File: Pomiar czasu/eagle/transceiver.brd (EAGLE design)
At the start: 100.3 x 59.6 mm, 61 parts, among them IC1 MEGA8-AI, U1 RFM69HW

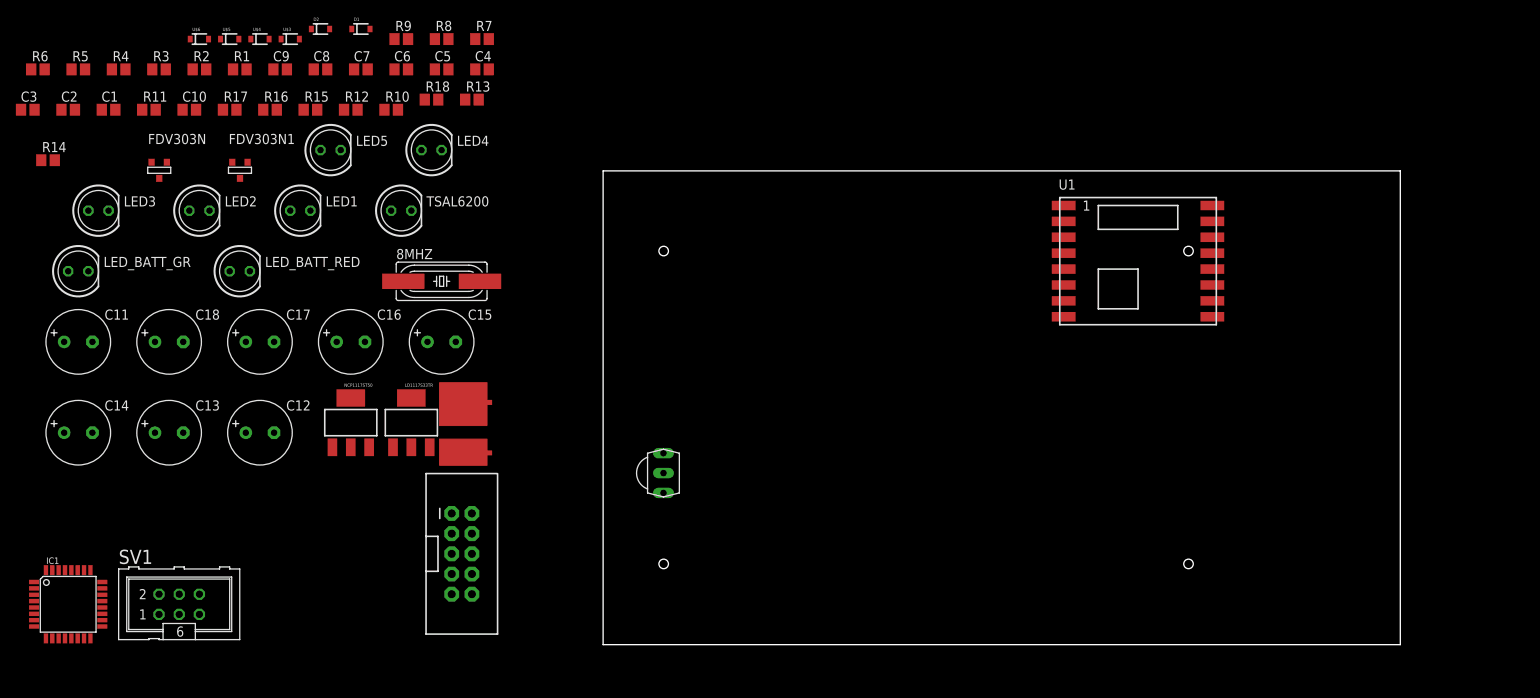
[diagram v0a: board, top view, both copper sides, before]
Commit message: defines added, demo program
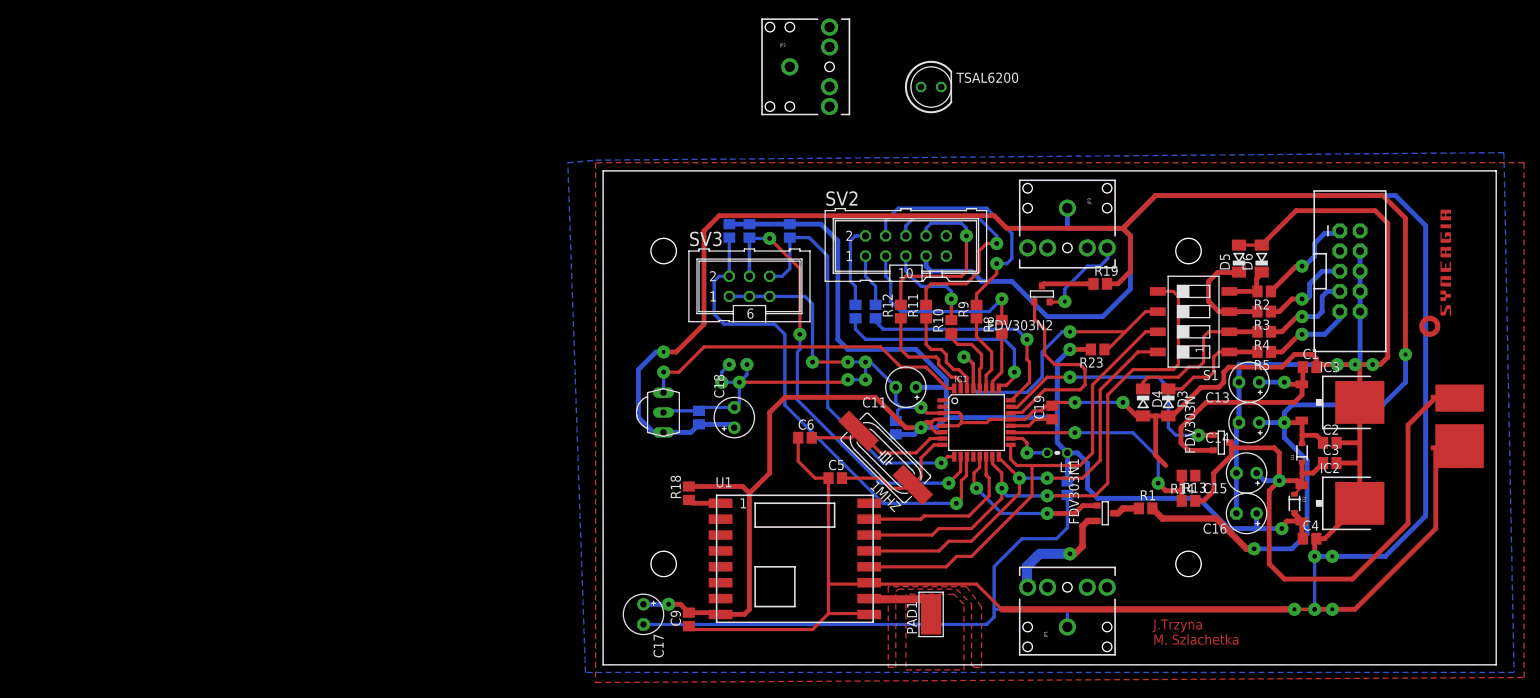
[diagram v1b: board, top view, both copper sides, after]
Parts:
- removed 8MHZ: (no value), crystal:HC49UP
- removed C12: (no value), resistor:E3,5-8
- removed C8: (no value), resistor:C0805
- removed LD1117S33TR: 3.3V, SparkFun-PowerIC:SOT223
- removed LED1, LED2, LED3, LED4, LED5, LED_BATT_GR, LED_BATT_RED: (no value), led:LED5MM
- removed NCP1117ST50: 5V, SparkFun-PowerIC:SOT223
- removed SV1: (no value), con-harting-ml:ML6
- removed U$4, U$5, U$6: (no value), SparkFun:SOD-323
- added 1MHZ: (no value), crystal:HC49UP
- added C19, C20: (no value), resistor:C0805
- added D3, D4, D5, D6: (no value), diode:SOD80C
- added FDV303N2: (no value), zetex:SOT-23
- added IC2: LF33, linear:TO252
- added IC3: LF50, linear:TO252
- added JP1, JP2, JP3: (no value), SparkFun-Connectors:AUDIO-JACK
- added L1: (no value), resistor:0204V
- added PAD1: WIREPADSMD5-2,5, wirepad:5-2,5
- added R19: (no value), resistor:R0805
- added R23: 1k, resistor:R0805
- added S1: SWS004, smd-special:SMS-004
- added SV2: (no value), con-harting-ml:ML10
- added SV3: (no value), con-harting-ml:ML6
- C11, C13, C14, C15, C16, C17, C18: device resistor:E3,5-8 -> rcl:E2,5-5
- R1: value (none) -> 36,5R
- R10, R12, R6, R7, R8, R9: value (none) -> 1.2k
- R11: value (none) -> 1,2k
- R15, R16, R17: value (none) -> 10k
- U$3: device SparkFun:SOD-323 -> synergia_logo:SYNERGIA_16MM
- moved C3 169.8 mm to (91.4, 22.9)
- moved C2 164.2 mm to (91.4, 25.4)
- moved C1 154.6 mm to (88.9, 34.9)
- moved R5 153.4 mm to (83.2, 36.8), turned to 180 degrees
- moved U$3 150.8 mm to (106.7, 38.7), turned to 90 degrees
- moved R14 148.9 mm to (73.7, 21.3), turned to 180 degrees
- moved R4 147.9 mm to (83.2, 39.4), turned to 180 degrees
- moved C14 147.3 mm to (81.3, 27.9), turned to 180 degrees
- moved R3 142.4 mm to (83.2, 41.9), turned to 180 degrees
- moved FDV303N 138.0 mm to (77.8, 25.4), turned to 90 degrees
- moved R2 136.9 mm to (83.2, 44.5), turned to 180 degrees
- moved D2 136.3 mm to (87.0, 17.8), turned to 270 degrees
- moved C13 136.0 mm to (81.3, 33.0), turned to 180 degrees
- moved D1 129.9 mm to (87.9, 24.1), turned to 90 degrees
- moved R1 126.7 mm to (68.3, 17.1)
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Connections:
- removed net GND: C1.2, C10.1, C11.-, C12.-, C13.-, C14.-, C15.-, C16.-, C17.-, C18.-, C2.2, C3.2, C4.2, C5.1, C6.1, C7.1, C8.1, C9.1, FDV303N1.2, IC1.21, IC1.3, IC1.5, LD1117S33TR.1, LED1.K, LED2.K, LED3.K, LED4.K, LED5.K, LED_BATT_GR.K, LED_BATT_RED.K, NCP1117ST50.1, R14.1, TSOP.GND, U$1.P$NEG, U$2.10, U$2.4, U$2.6, U$2.8, U$3.2, U$4.2, U$5.2, U$6.2, U1.11, U1.9
- removed net N$18: R15.1, SV1.2
- removed net N$19: R16.1, SV1.4
- removed net N$20: R17.1, SV1.6
- new net $1S1: C1.2, C10.1, C11.-, C13.-, C14.-, C15.-, C16.-, C17.-, C18.-, C19.2, C2.2, C20.2, C3.2, C4.2, C5.1, C6.1, C7.1, C9.1, D3.A, D4.A, D5.A, D6.A, IC1.21, IC1.3, IC1.5, IC2.3, IC3.3, JP1.SLEEVE, JP3.SLEEVE, R14.1, SV2.7, SV3.1, SV3.3, SV3.5, TSOP.GND, U$1.P$NEG, U$2.10, U$2.4, U$2.6, U$2.8, U1.11, U1.9
- new net LED_STRIPE: FDV303N2.3, IC1.22
- new net N$22: JP2.SLEEVE, TSAL6200.K
- new net N$23: FDV303N1.2, JP1.RING
- new net N$24: FDV303N2.2, JP3.RING
- new net N$25: FDV303N2.1, R19.1
- new net N$26: C19.1, IC1.20
- new net N$27: C15.+, C3.1, D1.1, D2.1, FDV303N.1, IC2.1, R13.2, U$1.P$POS
- new net N$28: PAD1.1, U1.10
- new net N$29: D6.C, R2.2, S1.4
- new net N$30: D5.C, R3.2, S1.3
- new net N$31: D4.C, R4.2, S1.2
- new net N$32: D3.C, R5.2, S1.1
- net +3V3: now also C20.1, IC2.2, L1.1, R23.2; no longer C12.+, C8.2, IC1.18, IC1.20, LD1117S33TR.2
- net +5V: now also C14.+, C2.1, D1.2, IC3.2, R19.2; no longer FDV303N.2
- net MISO: now also S1.8; no longer R5.2, U$5.1
- net MOSI: now also S1.5; no longer R2.2, U$4.1
- net N$1: now also FDV303N.2, IC3.1; no longer D1.1, NCP1117ST50.3, R13.2, U$1.P$POS
- net N$10: now also SV2.2; no longer LED2.A
- net N$11: now also SV2.3; no longer LED3.A
- net N$12: now also SV2.4; no longer LED4.A
- net N$13: now also SV2.5; no longer LED5.A
- net N$14: now also 1MHZ.2; no longer 8MHZ.2
- net N$15: now also 1MHZ.1; no longer 8MHZ.1
- net N$16: now also SV2.6; no longer LED_BATT_GR.A
- net N$17: now also SV2.8; no longer LED_BATT_RED.A
- net N$2: now also IC1.18, L1.2; no longer C14.+, C15.+, C2.1, C3.1, D1.2, D2.1, FDV303N.1, LD1117S33TR.3, NCP1117ST50.2
- net N$3: now also JP2.RING, TSAL6200.A; no longer FDV303N1.1, TSAL6200.K
- net N$8: now also FDV303N1.1; no longer TSAL6200.A
- net N$9: now also SV2.1; no longer LED1.A
- net RESET: now also R23.1, S1.6; no longer R3.2, U$3.1
- net SCK: now also S1.7; no longer R4.2, U$6.1
- net SWITCH_DOWN: now also R15.1, SV3.2; no longer SV1.1
- net SWITCH_OK: now also R16.1, SV3.4; no longer SV1.3
- net SWITCH_UP: now also R17.1, SV3.6; no longer SV1.5
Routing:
- net $1S1: track 0.00 -> 679.6 mm, vias 0 -> 20
- net +5V: track 0.00 -> 232.1 mm, vias 0 -> 4
- net +3V3: track 0.00 -> 210.7 mm, vias 0 -> 4
- net N$27: track 0.00 -> 83.6 mm, vias 0 -> 1
- net MOSI: track 0.00 -> 71.9 mm, vias 0 -> 2
- net SWITCH_DOWN: track 0.00 -> 63.1 mm, vias 0 -> 1
- net SWITCH_OK: track 0.00 -> 61.5 mm, vias 0 -> 3
- net SCK: track 0.00 -> 60.7 mm
- net MISO: track 0.00 -> 57.0 mm, vias 0 -> 2
- net SWITCH_UP: track 0.00 -> 50.8 mm, vias 0 -> 1
- net TSOP_OUT: track 0.00 -> 42.6 mm, vias 0 -> 1
- net RESET: track 0.00 -> 42.3 mm, vias 0 -> 2
- net N$1: track 0.00 -> 33.5 mm, vias 0 -> 1
- net 5V_ENABLE: track 0.00 -> 33.0 mm, vias 0 -> 2
- net N$12: track 0.00 -> 31.3 mm, vias 0 -> 1
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- added copper zone on layer 1, net $1S1
- added copper zone on layer 16, net $1S1
- added copper zone on layer 1, net N$18
- added copper zone on layer 1, net N$28
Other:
- board size 100.3 x 59.6 mm -> 112.4 x 62.2 mm
- board text added: "J.Trzyna M. Szlachetka"
